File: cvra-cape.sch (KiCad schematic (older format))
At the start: 5 parts

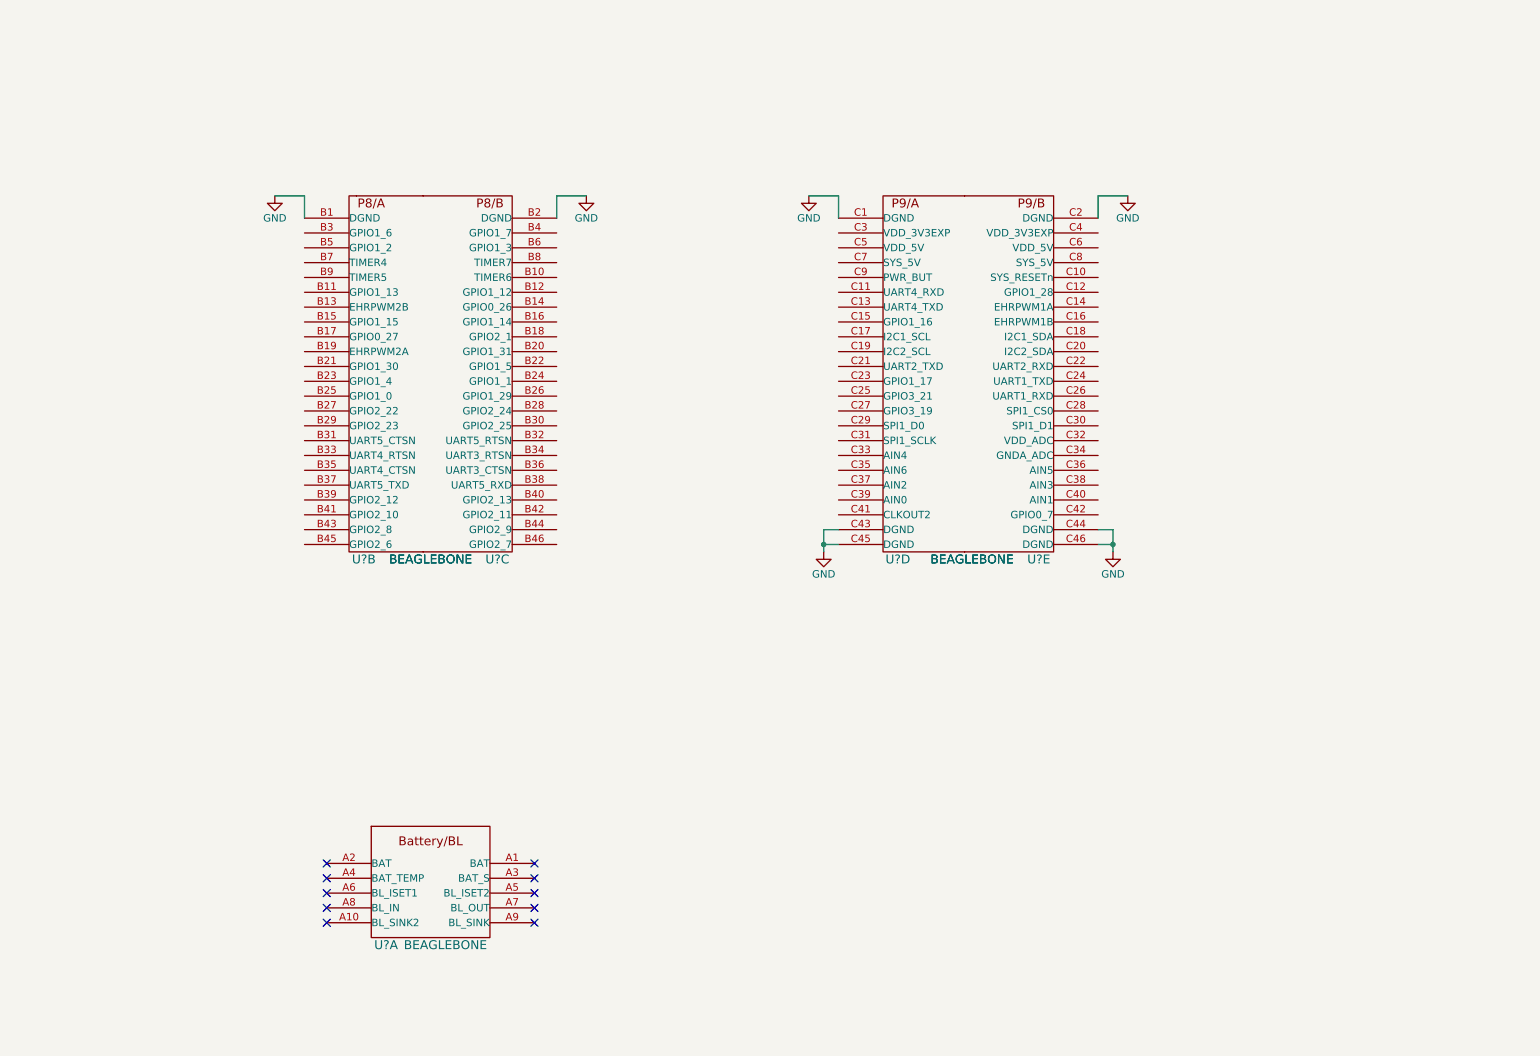
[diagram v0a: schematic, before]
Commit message: Add PWM outputs
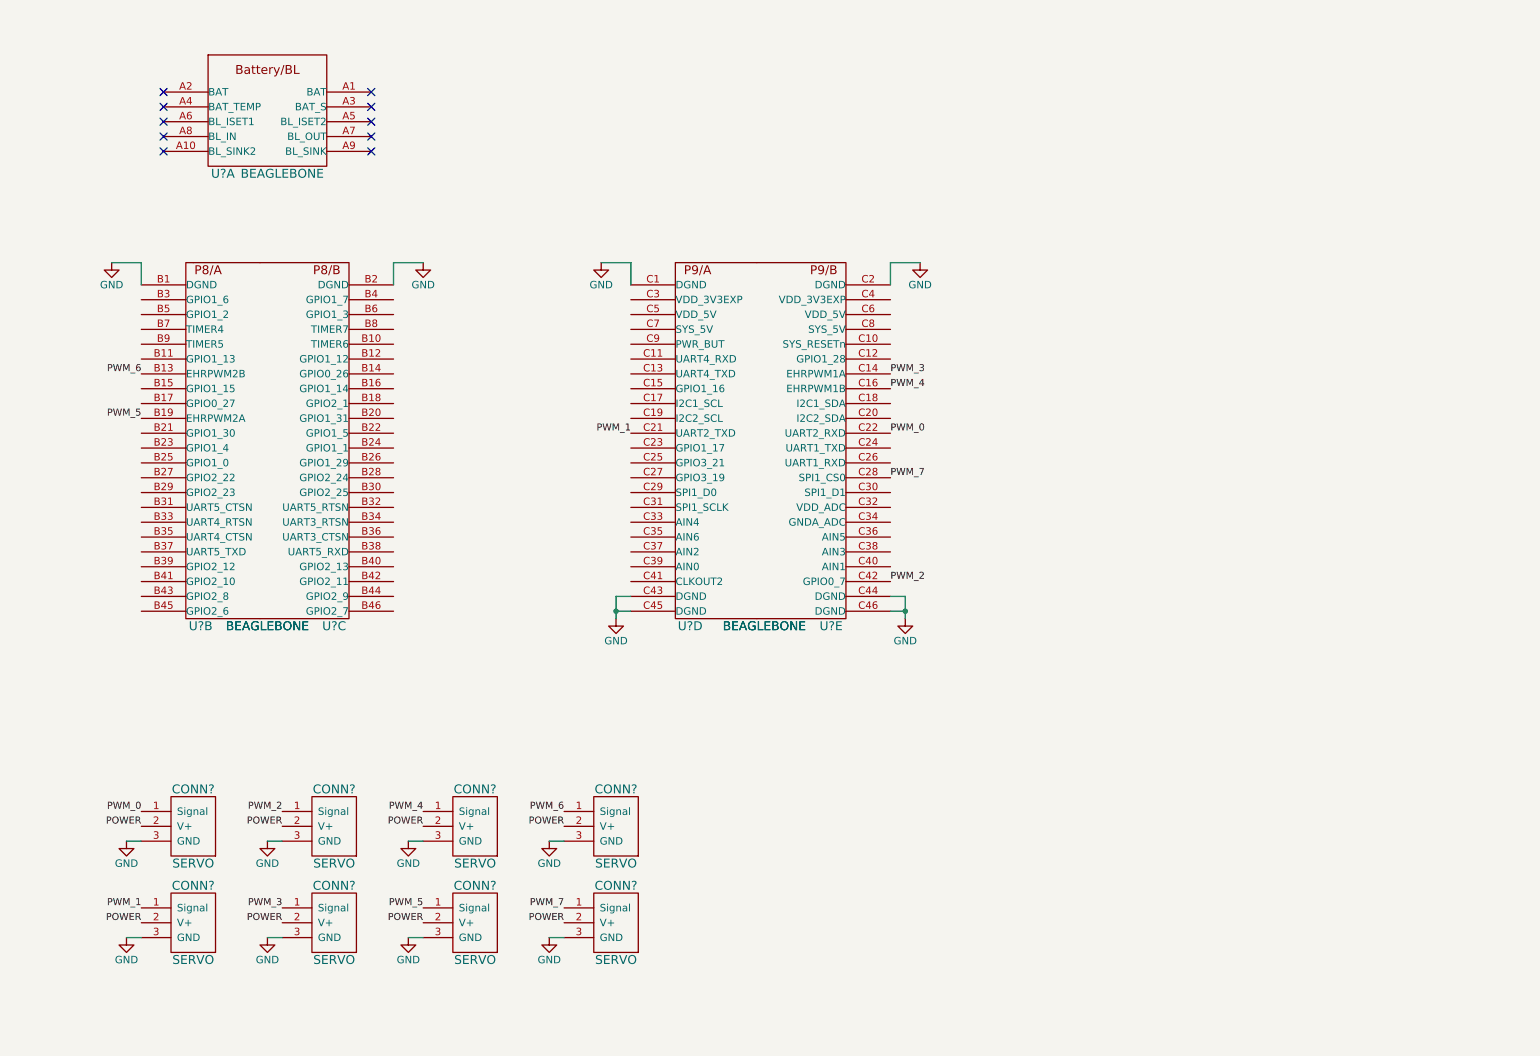
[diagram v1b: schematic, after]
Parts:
- added CONN? (x8): SERVO, symbol SERVO
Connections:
- net GND: now also CONN?.3 (GND), CONN?.3 (GND), CONN?.3 (GND), CONN?.3 (GND), CONN?.3 (GND), CONN?.3 (GND), CONN?.3 (GND), CONN?.3 (GND)
- net PWM_6: now reaches U?.B13 (EHRPWM2B)
- net PWM_6: now also CONN?.1 (Signal)
- net PWM_5: now reaches U?.B19 (EHRPWM2A)
- net PWM_5: now also CONN?.1 (Signal)
- net PWM_1: now reaches U?.C21 (UART2_TXD)
- net PWM_1: now also CONN?.1 (Signal)
- net PWM_3: now reaches U?.C14 (EHRPWM1A)
- net PWM_3: now also CONN?.1 (Signal)
- net PWM_4: now reaches U?.C16 (EHRPWM1B)
- net PWM_4: now also CONN?.1 (Signal)
- net PWM_0: now reaches U?.C22 (UART2_RXD)
- net PWM_0: now also CONN?.1 (Signal)
- net PWM_7: now reaches U?.C28 (SPI1_CS0)
- net PWM_7: now also CONN?.1 (Signal)
- net PWM_2: now reaches U?.C42 (GPIO0_7)
- net PWM_2: now also CONN?.1 (Signal)
- new net POWER: CONN?.2 (V+), CONN?.2 (V+), CONN?.2 (V+), CONN?.2 (V+), CONN?.2 (V+), CONN?.2 (V+), CONN?.2 (V+), CONN?.2 (V+)
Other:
- moved on the sheet: U?A, U?B, U?C, U?D, U?E

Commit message: Add CAN interfaces
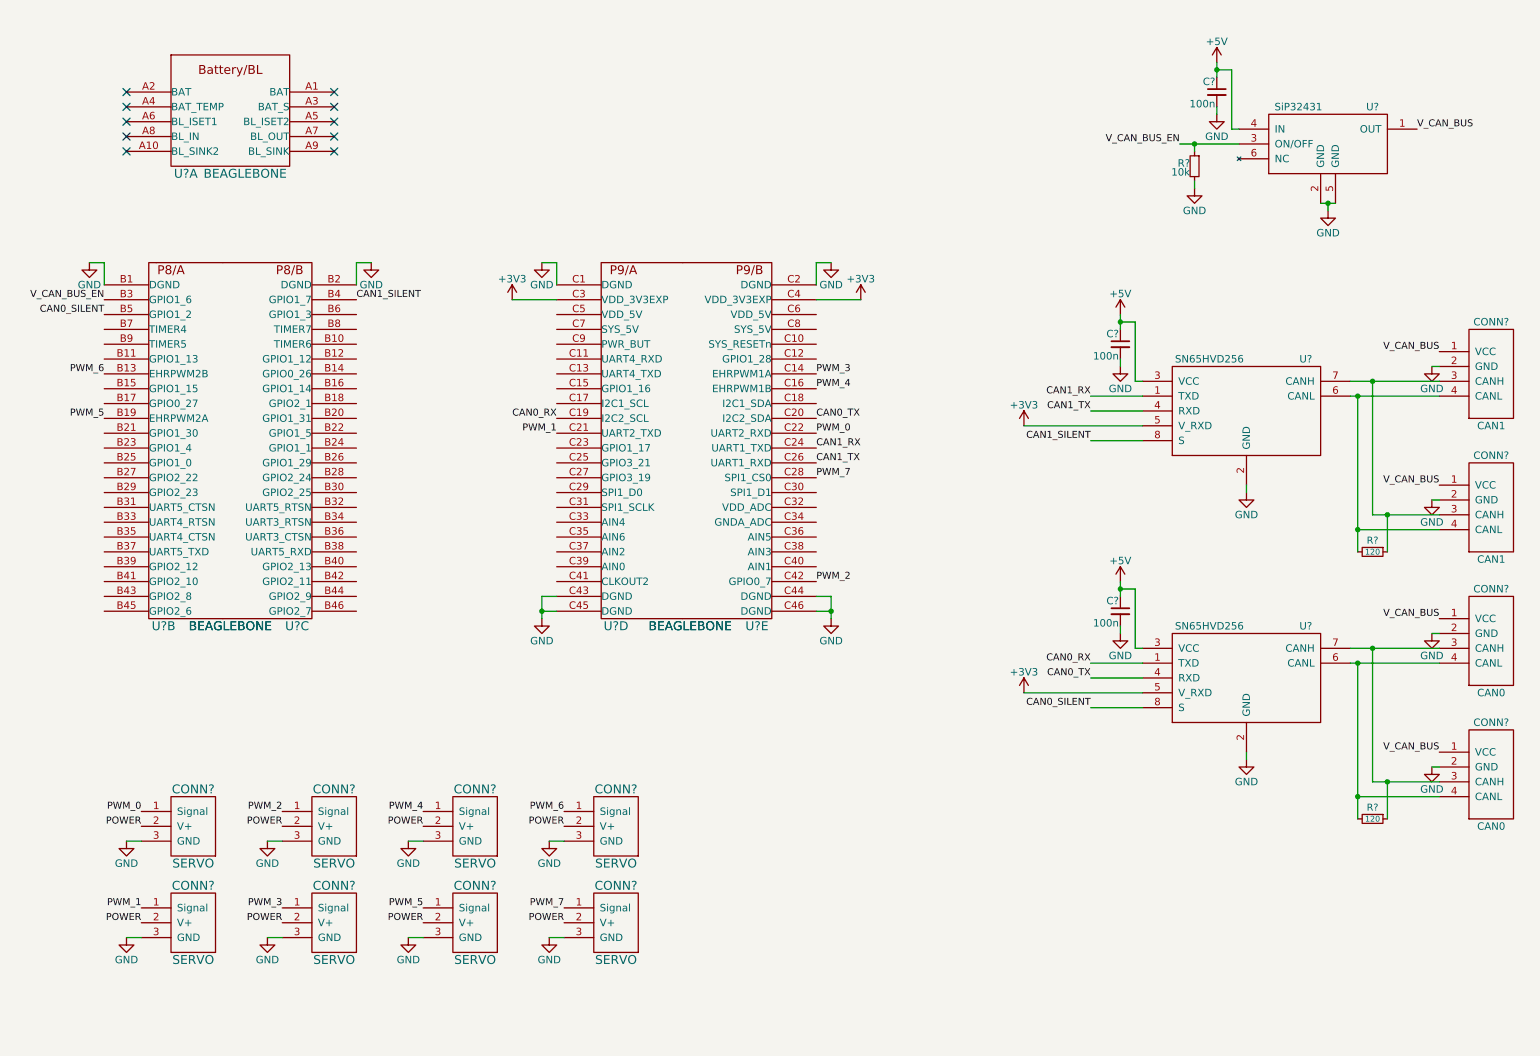
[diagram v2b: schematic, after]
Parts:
- added C? (x3): 100n, symbol C_Small
- added CONN? (x2): CAN1, MODULE, symbol CAN
- added CONN? (x2): CAN0, MODULE, symbol CAN
- added R? (x2): 120, symbol R_Small
- added R?: 10k, symbol R_Small
- added U? (x2): SN65HVD256, MODULE, symbol SN65HVD256
- added U?: SiP32431, MODULE, symbol SiP32431
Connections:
- net GND: now also C?.2, C?.2, C?.2, CONN?.2 (GND), CONN?.2 (GND), CONN?.2 (GND), CONN?.2 (GND), CONN?.MECH (GND), CONN?.MECH (GND), CONN?.MECH (GND), CONN?.MECH (GND), R?.2, U?.2 (GND), U?.2 (GND), U?.2 (GND), U?.5 (GND)
- net V_CAN_BUS_EN: now reaches U?.B3 (GPIO1_6)
- net V_CAN_BUS_EN: now also R?.1, U?.3 (ON/OFF)
- net CAN0_SILENT: now reaches U?.B5 (GPIO1_2)
- net CAN0_SILENT: now also U?.8 (S)
- net CAN1_SILENT: now reaches U?.B4 (GPIO1_7)
- net CAN1_SILENT: now also U?.8 (S)
- net CAN0_RX: now reaches U?.C19 (I2C2_SCL)
- net CAN0_RX: now also U?.1 (TXD)
- net +3V3: now reaches U?.C3 (VDD_3V3EXP)
- net +3V3: now also U?.C4 (VDD_3V3EXP), U?.5 (V_RXD), U?.5 (V_RXD)
- net CAN0_TX: now reaches U?.C20 (I2C2_SDA)
- net CAN0_TX: now also U?.4 (RXD)
- net CAN1_RX: now reaches U?.C24 (UART1_TXD)
- net CAN1_RX: now also U?.1 (TXD)
- net CAN1_TX: now reaches U?.C26 (UART1_RXD)
- net CAN1_TX: now also U?.4 (RXD)
- new net: CONN?.4 (CANL), CONN?.4 (CANL), R?.2, U?.6 (CANL) (x2)
- new net: CONN?.3 (CANH), CONN?.3 (CANH), R?.1, U?.7 (CANH) (x2)
- new net +5V: C?.1, C?.1, C?.1, U?.3 (VCC), U?.3 (VCC), U?.4 (IN)
- new net V_CAN_BUS: CONN?.1 (VCC), CONN?.1 (VCC), CONN?.1 (VCC), CONN?.1 (VCC), U?.1 (OUT)
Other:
- moved on the sheet: U?A, U?B, U?C, U?D, U?E

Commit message: Add PWM chip and servo outputs
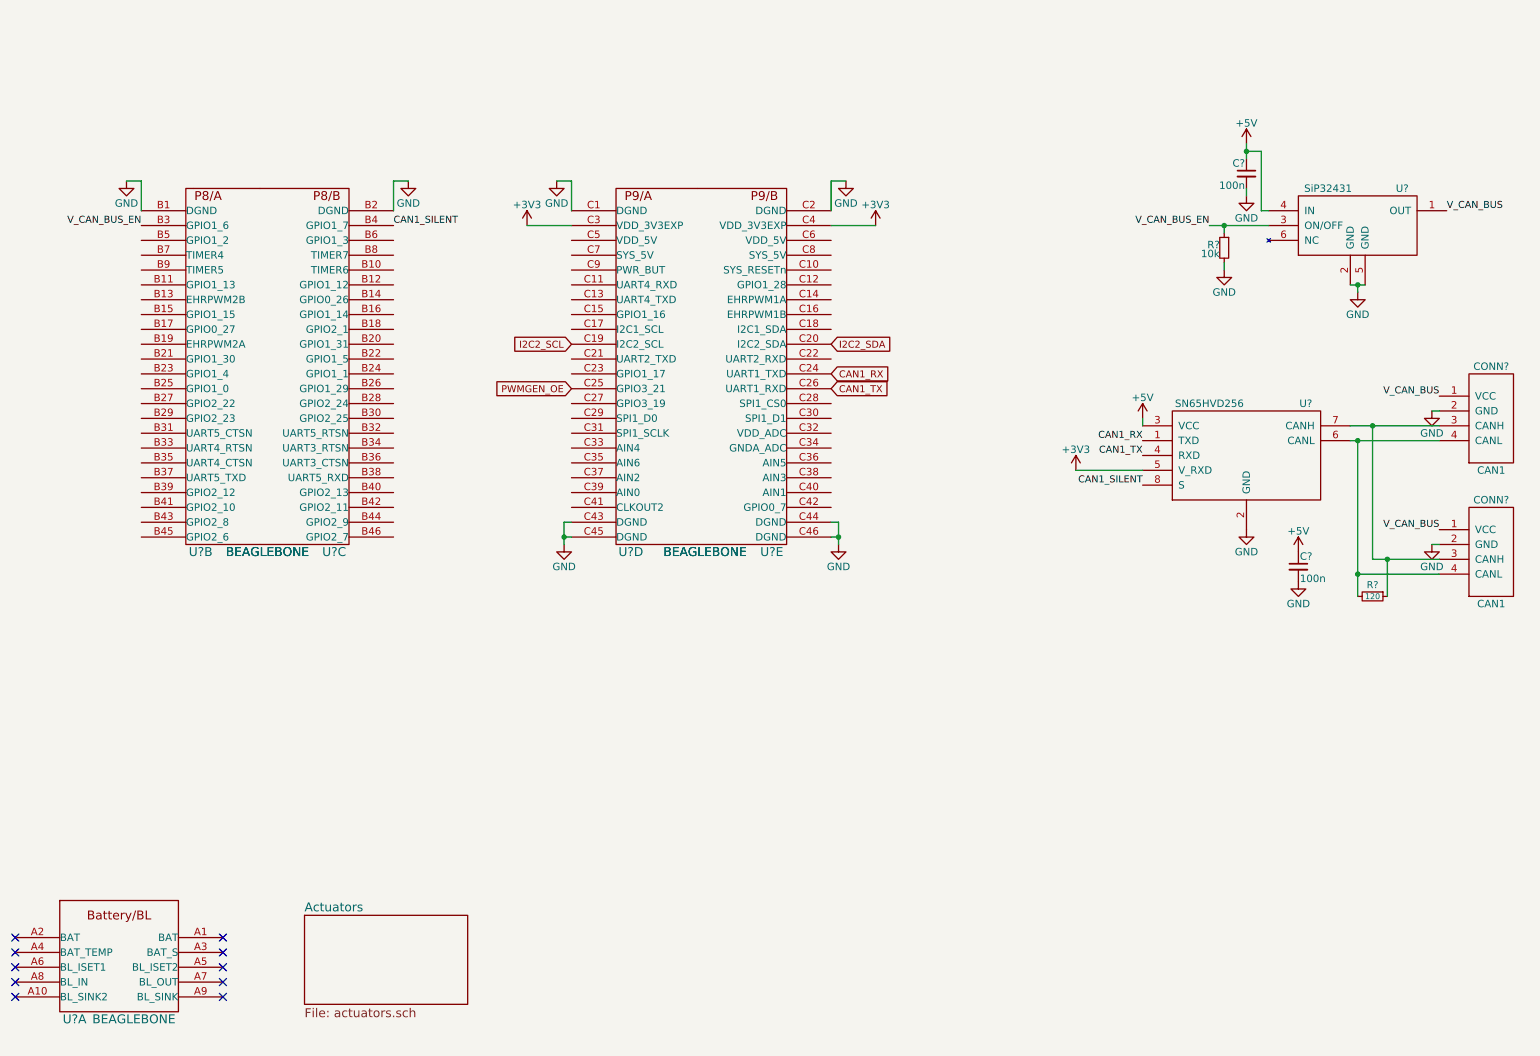
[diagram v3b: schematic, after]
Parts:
- removed C? (x2): 100n, symbol C_Small
- removed CONN? (x8): SERVO, symbol SERVO
- removed CONN? (x2): CAN0, MODULE, symbol CAN
- removed R?: 120, symbol R_Small
- removed U?: SN65HVD256, MODULE, symbol SN65HVD256
- added C?: 100n, symbol C_Small
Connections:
- net +5V: now also C?.1
- net GND: now also C?.2
- net PWMGEN_OE: now reaches U?.C25 (GPIO3_21)
- net CAN0_RX renamed I2C2_SCL
- net CAN0_SILENT: no longer names the net of U?.B5 (GPIO1_2)
- net CAN0_TX renamed I2C2_SDA
- net PWM_0: no longer names the net of U?.C22 (UART2_RXD)
- net PWM_1: no longer names the net of U?.C21 (UART2_TXD)
- net PWM_2: no longer names the net of U?.C42 (GPIO0_7)
- net PWM_3: no longer names the net of U?.C14 (EHRPWM1A)
- net PWM_4: no longer names the net of U?.C16 (EHRPWM1B)
- net PWM_5: no longer names the net of U?.B19 (EHRPWM2A)
- net PWM_6: no longer names the net of U?.B13 (EHRPWM2B)
- net PWM_7: no longer names the net of U?.C28 (SPI1_CS0)
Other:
- moved on the sheet: C?, CONN?, R?, U?, U?A, U?B, U?C, U?D, U?E

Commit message: Add power from CAN bus and switch to hierarchical labelling
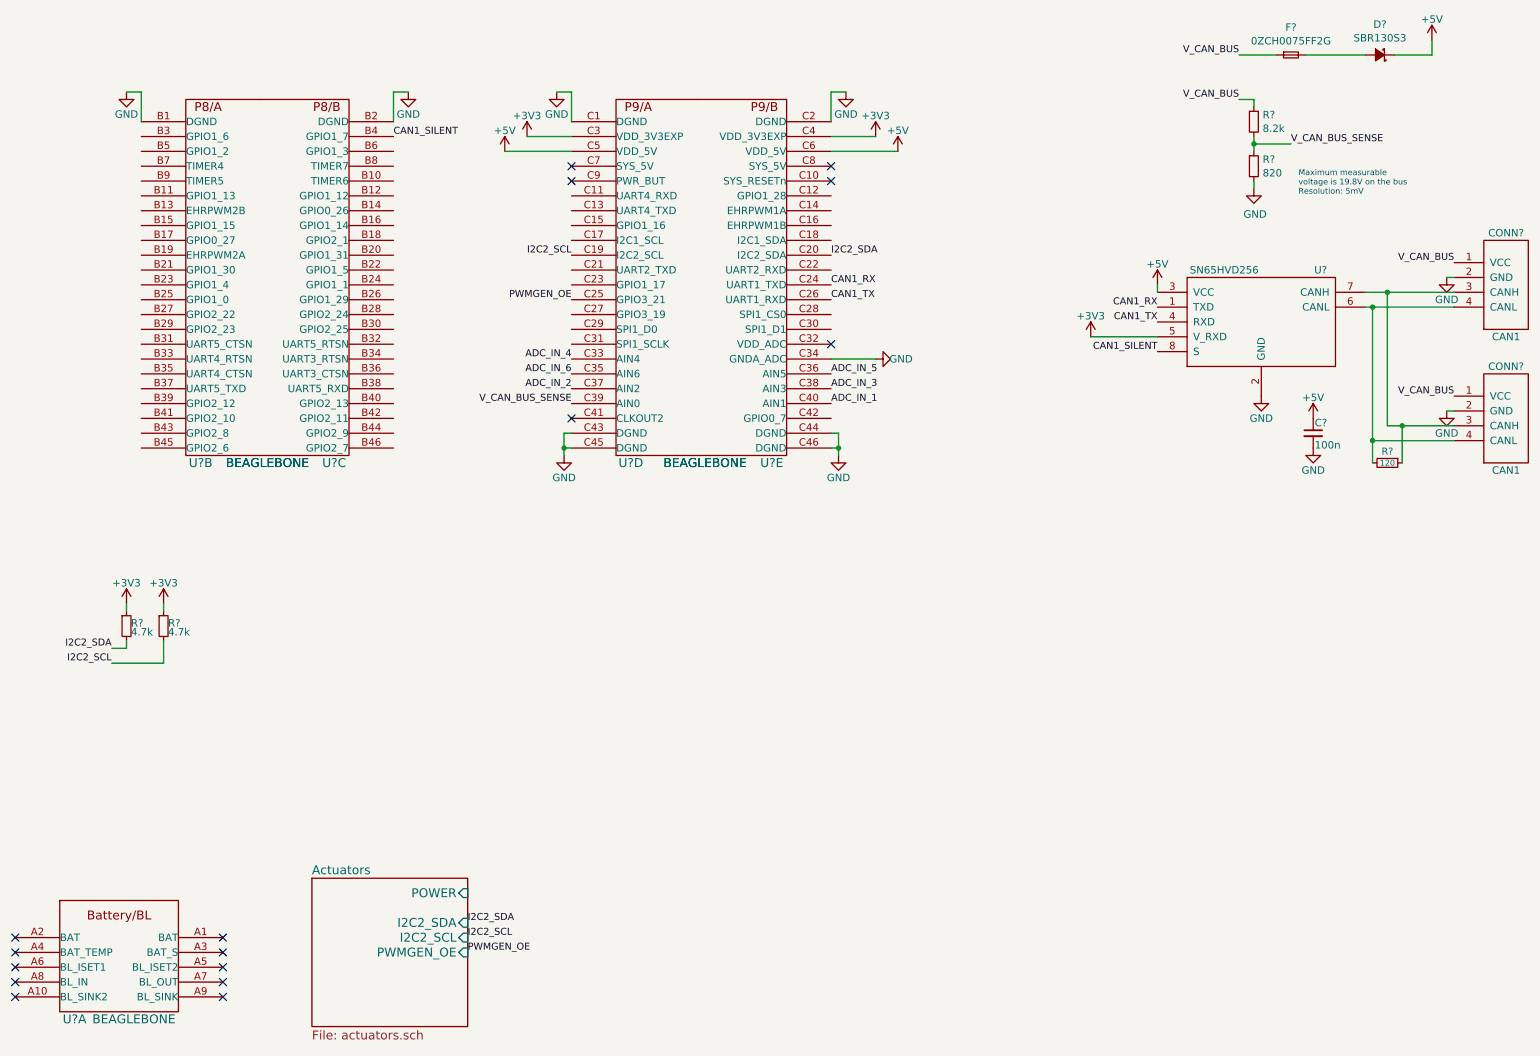
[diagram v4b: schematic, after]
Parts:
- removed C?: 100n, symbol C_Small
- removed R?: 10k, symbol R_Small
- removed U?: SiP32431, MODULE, symbol SiP32431
- added D?: SBR130S3, symbol D_Schottky_Small
- added F?: 0ZCH0075FF2G, symbol F_Small
- added R? (x2): 4.7k, symbol R_Small
- added R?: 8.2k, symbol R_Small
- added R?: 820, symbol R_Small
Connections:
- net +3V3: now also R?.1, R?.1
- net +5V: now also U?.C5 (VDD_5V), U?.C6 (VDD_5V), D?.1 (K)
- net GND: now also U?.C34 (GNDA_ADC), R?.2
- net I2C2_SCL: now also R?.2
- net I2C2_SDA: now also R?.2
- net V_CAN_BUS: now also F?.1, R?.1
- net ADC_IN_4: now reaches U?.C33 (AIN4)
- net ADC_IN_6: now reaches U?.C35 (AIN6)
- net ADC_IN_2: now reaches U?.C37 (AIN2)
- net V_CAN_BUS_SENSE: now reaches U?.C39 (AIN0)
- net V_CAN_BUS_SENSE: now also R?.1, R?.2
- net ADC_IN_5: now reaches U?.C36 (AIN5)
- net ADC_IN_3: now reaches U?.C38 (AIN3)
- net ADC_IN_1: now reaches U?.C40 (AIN1)
- net V_CAN_BUS_EN: no longer names the net of U?.B3 (GPIO1_6)
- new net: D?.2 (A), F?.2
- no-connect marks 10 -> 16
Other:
- note added: "Maximum measurable \nvoltage is 19.8V on the bus\nResolution: 5mV"
- moved on the sheet: C?, CONN?, R?, U?, U?B, U?C, U?D, U?E
